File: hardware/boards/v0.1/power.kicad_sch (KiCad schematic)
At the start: 66 parts, among them IC3 SP3401-02UTG, J2 USB, U20 TPS62A02ADRLR, U23 BQ21040DBV, U30 FUSB307BVMPX, U31 TPS22929D, U32 LTC2942, U36 STM6601GU2BDM6F, U39 TPS61252DSG, U40 MIC2017YM6

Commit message: chore: schematic cleanup
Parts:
- D19: JLC (none) -> C130719
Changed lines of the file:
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@@
 			)
 		)
-		(property "JLC" ""
+		(property "JLC" "C130719"
 			(at 250.19 82.55 0)
 			(effects
@@
 					(size 1.27 1.27)
 				)
+				(hide yes)
 			)
 		)
@@
 				)
 				(justify left)
-			)
-		)
-		(property "MANUFACTURER" ""
-			(at 250.19 82.55 0)
-			(effects
-				(font
-					(size 1.27 1.27)
-				)
-			)
-		)
-		(property "MAXIMUM_PACKAGE_HEIGHT" ""
-			(at 250.19 82.55 0)
-			(effects
-				(font
-					(size 1.27 1.27)
-				)
-			)
-		)
-		(property "Connector" ""
-			(at 250.19 82.55 0)
-			(effects
-				(font
-					(size 1.27 1.27)
-				)
 			)
 		)
@@
 					(size 1.27 1.27)
 				)
-			)
-		)
+				(hide yes)
+			)
+		)

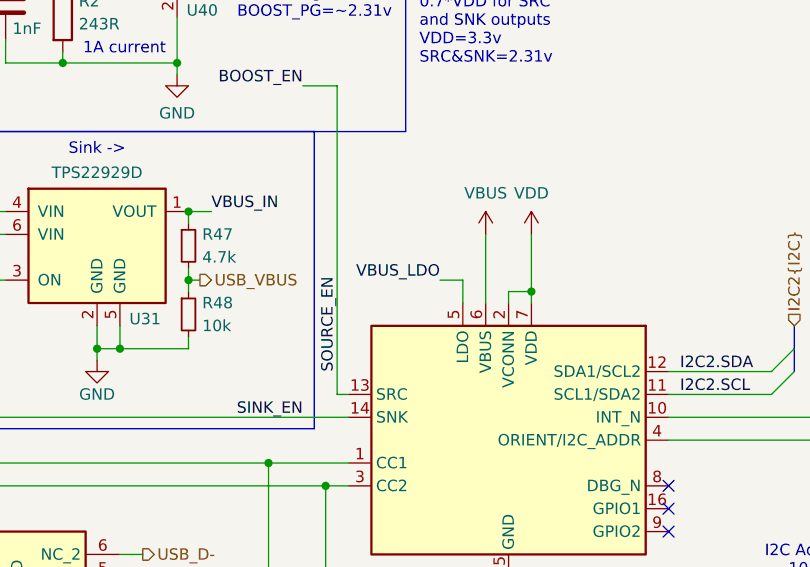
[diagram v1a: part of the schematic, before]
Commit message: feat: add LCD backlight control
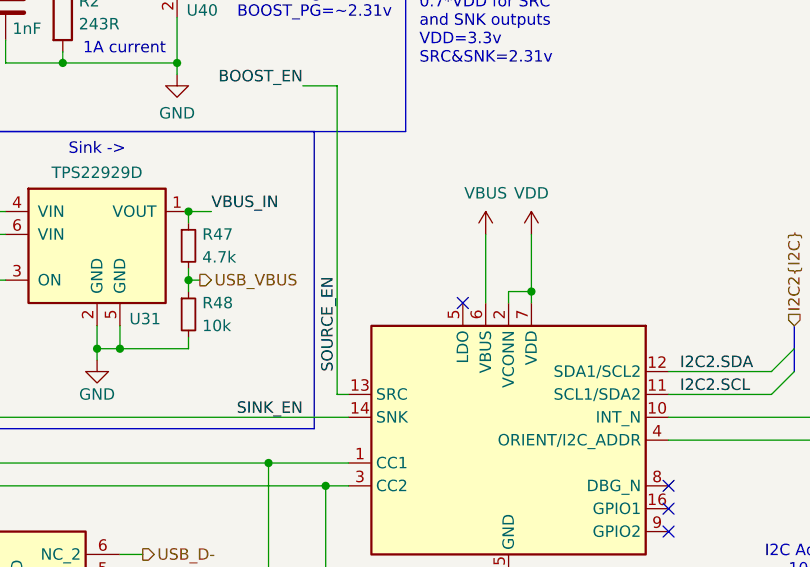
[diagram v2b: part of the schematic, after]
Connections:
- net VBUS_LDO: no longer names the net of U30.5 (LDO)
- no-connect marks 9 -> 10
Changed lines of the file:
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@@
 		(at 134.62 96.52)
+	)
+	(no_connect
+		(at 111.76 71.12)
 	)
 	(bus_entry
@@
 	(wire
 		(pts
-			(xy 109.22 68.58) (xy 111.76 68.58)
-		)
-		(stroke
-			(width 0)
-			(type default)
-		)
-	)
-	(wire
-		(pts
 			(xy 76.2 153.67) (xy 76.2 156.21)
 		)
@@
 		(pts
 			(xy 158.75 168.91) (xy 167.64 168.91)
-		)
-		(stroke
-			(width 0)
-			(type default)
-		)
-	)
-	(wire
-		(pts
-			(xy 111.76 71.12) (xy 111.76 68.58)
 		)
 		(stroke
@@
 		)
 	)
-	(label "VBUS_LDO"
-		(at 109.22 68.58 180)
-		(effects
-			(font
-				(size 1.27 1.27)
-			)
-			(justify right bottom)
-		)
-	)

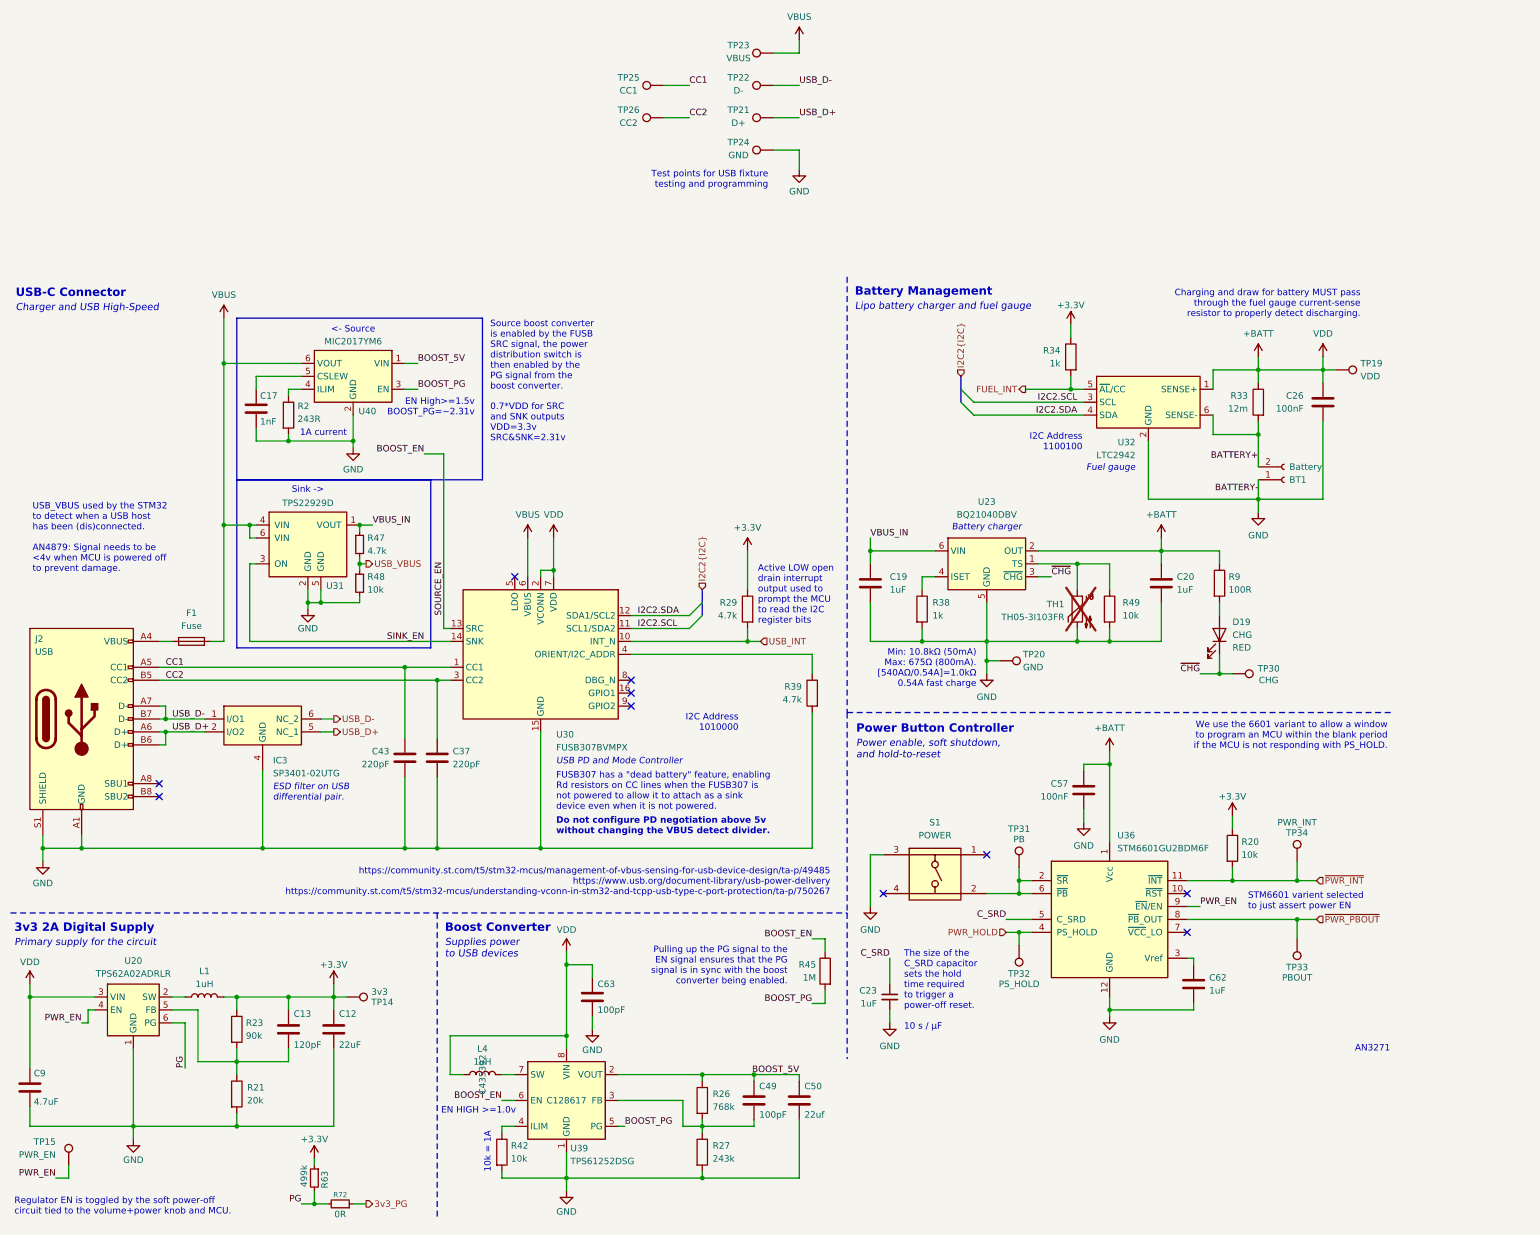
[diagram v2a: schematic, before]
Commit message: feat: add power LEDs and adjust layout
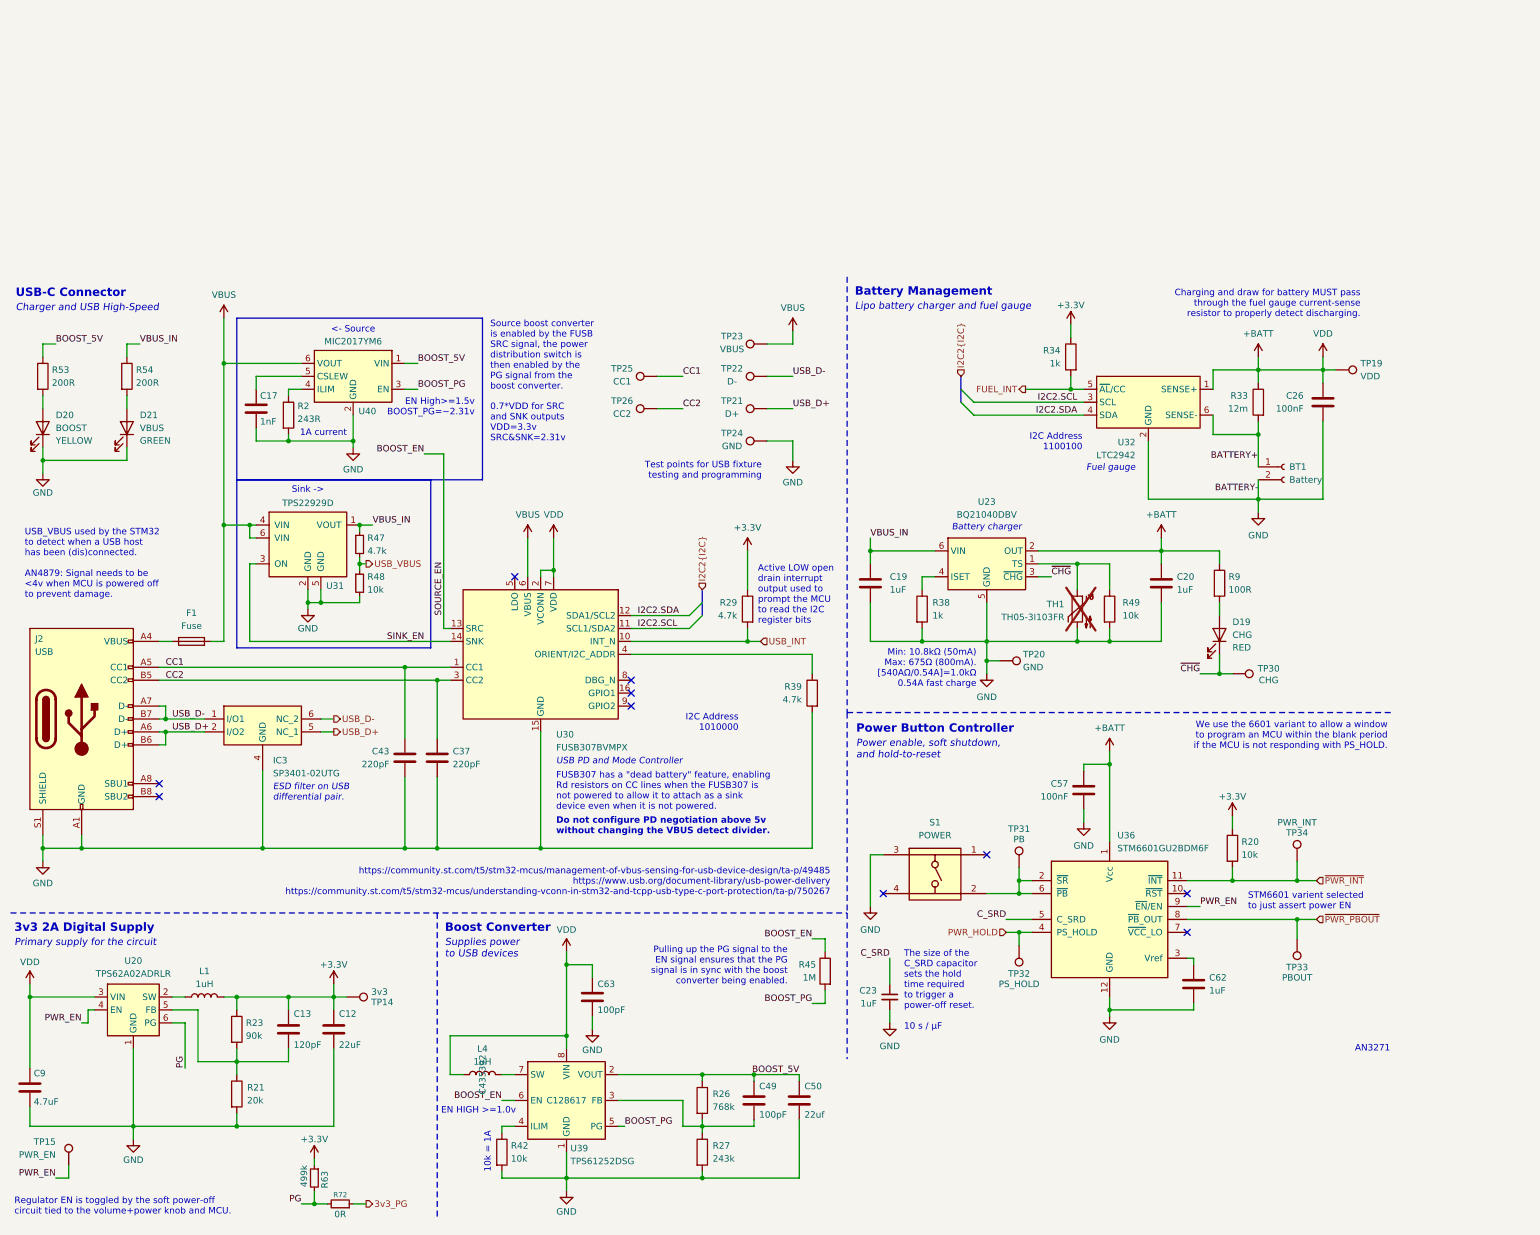
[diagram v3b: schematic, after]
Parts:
- added D20: BOOST, LED_SMD:LED_0805_2012Metric, symbol Device:LED
- added D21: VBUS, LED_SMD:LED_0805_2012Metric, symbol Device:LED
- added R53, R54: 200R, Resistor_SMD:R_0402_1005Metric, symbol Device:R
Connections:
- net BATTERY+: now also BT1.1 (Pin_1); no longer BT1.2 (Pin_2)
- net BOOST_5V: now also R53.1
- net GND: now also BT1.2 (Pin_2), D20.1 (K), D21.1 (K); no longer BT1.1 (Pin_1)
- net VBUS_IN: now also R54.1
- new net: D20.2 (A), R53.2
- new net: D21.2 (A), R54.2
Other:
- moved on the sheet: TP21, TP22, TP23, TP24, TP25, TP26

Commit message: feat: change charger, fuel gauge, and battery connector, re-route power system
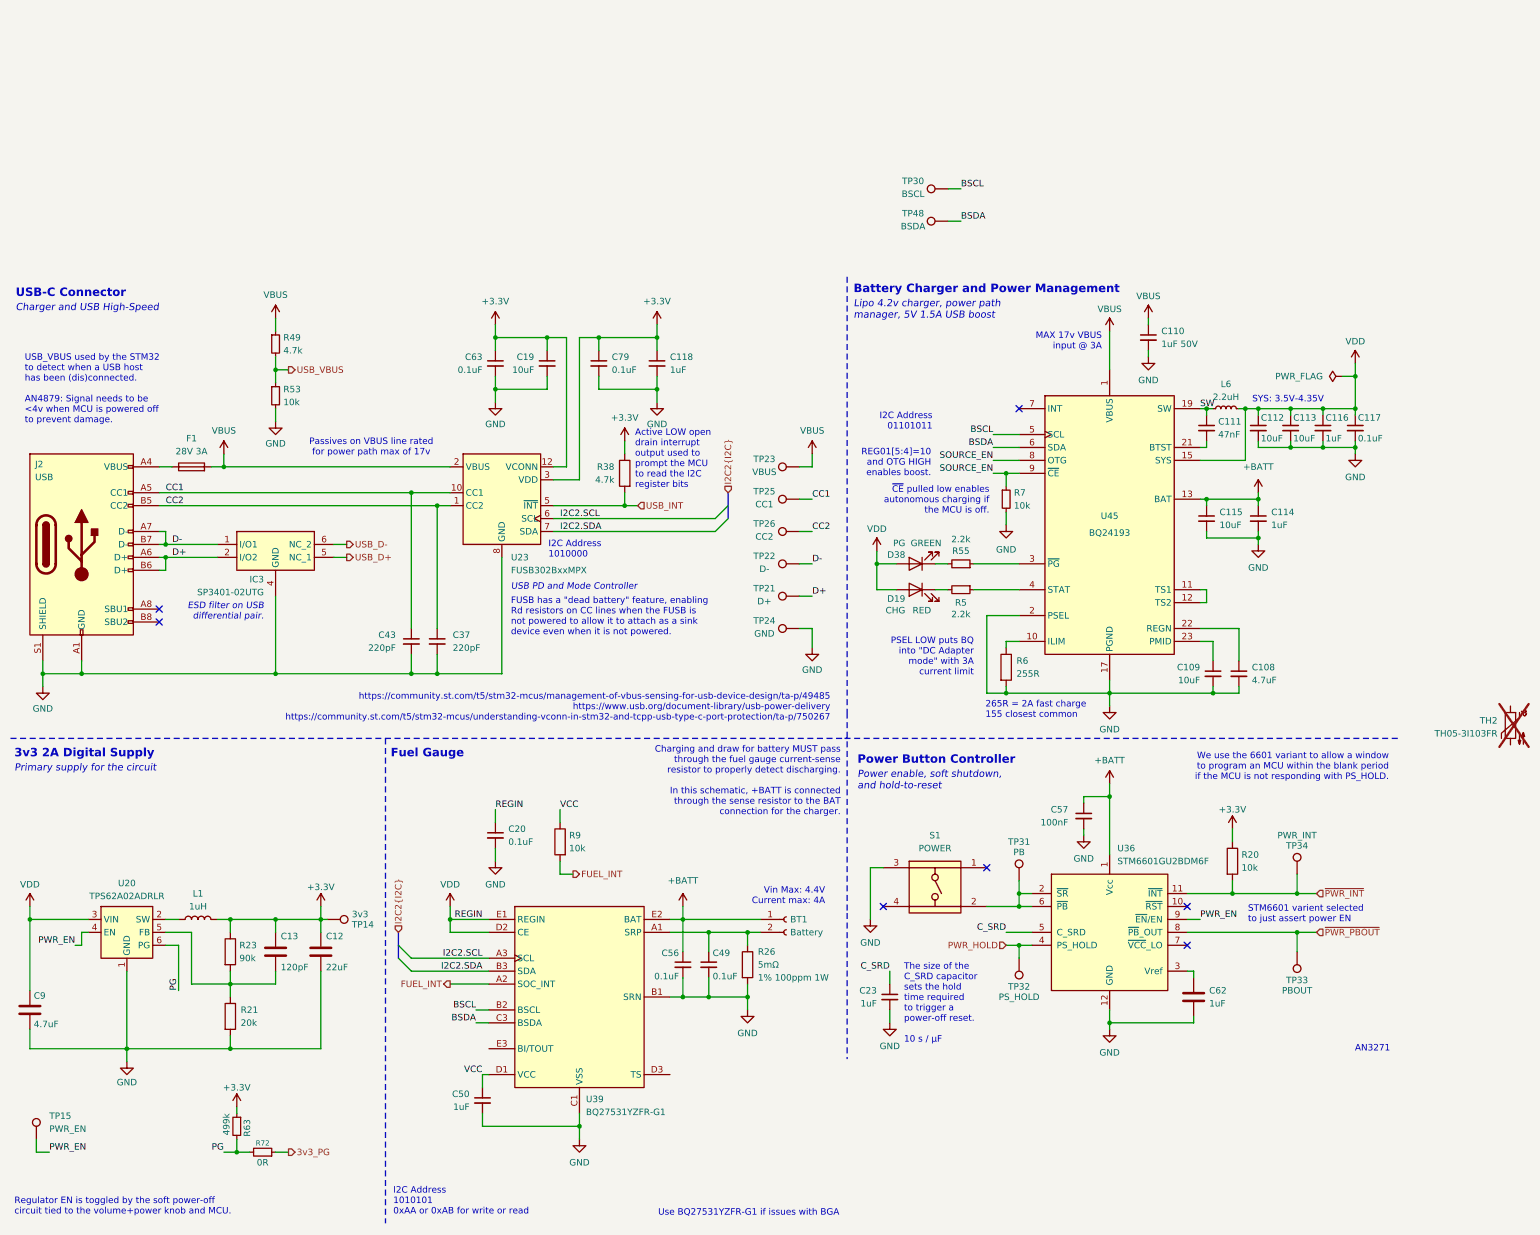
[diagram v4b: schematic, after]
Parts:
- removed C17: 1nF, Capacitor_SMD:C_0402_1005Metric, symbol Device:C
- removed C19, C20: 1uF, Capacitor_SMD:C_0805_2012Metric, symbol Device:C
- removed C26: 100nF, Capacitor_SMD:C_0603_1608Metric, symbol Device:C
- removed C49, C63: 100pF, Capacitor_SMD:C_0402_1005Metric, symbol Device:C
- removed C50: 22uf, Capacitor_SMD:C_0402_1005Metric, symbol Device:C
- removed D20: BOOST, LED_SMD:LED_0805_2012Metric, symbol Device:LED
- removed D21: VBUS, LED_SMD:LED_0805_2012Metric, symbol Device:LED
- removed L4: 1uH, Inductor_SMD:L_1008_2520Metric, symbol Device:L
- removed R2: 243R, Resistor_SMD:R_0402_1005Metric, symbol Device:R
- removed R27: 243k, Resistor_SMD:R_0402_1005Metric, symbol Device:R
- removed R29, R39: 4.7k, Resistor_SMD:R_0402_1005Metric, symbol Device:R
- removed R33: 12m, Resistor_SMD:R_1206_3216Metric_Pad1.30x1.75mm_HandSolder, symbol Device:R
- removed R34: 1k, Resistor_SMD:R_0603_1608Metric, symbol Device:R
- removed R42: 10k, Resistor_SMD:R_0402_1005Metric, symbol Device:R
- removed R45: 1M, Resistor_SMD:R_0402_1005Metric, symbol Device:R
- removed R47: 4.7k, Resistor_SMD:R_0402_1005Metric, symbol Device:R_Small
- removed R48: 10k, Resistor_SMD:R_0402_1005Metric, symbol Device:R_Small
- removed R49: 10k, Resistor_SMD:R_0805_2012Metric_Pad1.20x1.40mm_HandSolder, symbol Device:R
- removed R53, R54: 200R, Resistor_SMD:R_0402_1005Metric, symbol Device:R
- removed TH1: TH05-3I103FR, Resistor_SMD:R_0402_1005Metric_Pad0.72x0.64mm_HandSolder, symbol Device:Thermistor_NTC
- removed TP19: VDD, TestPoint:TestPoint_Pad_D1.0mm, symbol Connector:TestPoint
- removed TP20: GND, TestPoint:TestPoint_Pad_D1.0mm, symbol Connector:TestPoint
- removed U23: BQ21040DBV, Package_TO_SOT_SMD:SOT-23-6, symbol Battery_Management:BQ21040DBV
- removed U30: FUSB307BVMPX, Package_DFN_QFN:WQFN-16-1EP_3x3mm_P0.5mm_EP1.75x1.75mm, symbol Interface_USB:FUSB307BMPX
- removed U31: TPS22929D, Package_TO_SOT_SMD:SOT-23-6, symbol Power_Management:TPS22929D
- removed U32: LTC2942, Package_DFN_QFN:DFN-6-1EP_3x2mm_P0.5mm_EP1.65x1.35mm, symbol Battery_Management:LTC2942
- removed U39: TPS61252DSG, Package_SON:WSON-8-1EP_2x2mm_P0.5mm_EP0.9x1.6mm, symbol Regulator_Switching:TPS61252DSG
- removed U40: MIC2017YM6, Package_TO_SOT_SMD:SOT-23-6, symbol Power_Management:MIC2017YM6
- added C108: 4.7uF, Capacitor_SMD:C_0402_1005Metric, symbol Device:C_Small
- added C109, C112, C113, C115, C19: 10uF, Capacitor_SMD:C_0402_1005Metric, symbol Device:C_Small
- added C110: 1uF 50V, Capacitor_SMD:C_0603_1608Metric, symbol Device:C_Small
- added C111: 47nF, Capacitor_SMD:C_0402_1005Metric, symbol Device:C_Small
- added C114, C116, C118, C50: 1uF, Capacitor_SMD:C_0402_1005Metric, symbol Device:C_Small
- added C117, C20, C49, C56, C63, C79: 0.1uF, Capacitor_SMD:C_0402_1005Metric, symbol Device:C_Small
- added D38: PG, LED_SMD:LED_0805_2012Metric, symbol Device:LED
- added L6: 2.2uH, Inductor_SMD:L_0805_2012Metric, symbol Device:L_Small
- added R49: 4.7k, Resistor_SMD:R_0402_1005Metric, symbol Device:R_Small
- added R5, R55: 2.2k, Resistor_SMD:R_0402_1005Metric, symbol Device:R_Small
- added R53, R7: 10k, Resistor_SMD:R_0402_1005Metric, symbol Device:R_Small
- added R6: 255R, Resistor_SMD:R_0805_2012Metric_Pad1.20x1.40mm_HandSolder, symbol Device:R
- added TH2: TH05-3I103FR, Resistor_SMD:R_0402_1005Metric_Pad0.72x0.64mm_HandSolder, symbol Device:Thermistor_NTC
- added TP48: BSDA, TestPoint:TestPoint_Pad_D1.0mm, symbol Connector:TestPoint
- added U23: FUSB302BxxMPX, Package_DFN_QFN:WQFN-14-1EP_2.5x2.5mm_P0.5mm_EP1.45x1.45mm, symbol lethalbit:FUSB302B
- added U39: BQ27531YZFR-G1, pocket_synth:BGA15C50P3X5_196X261X63, symbol pocket_synth:BQ27531-G1
- added U45: BQ24193, Package_DFN_QFN:VQFN-24-1EP_4x4mm_P0.5mm_EP2.5x2.5mm_ThermalVias, symbol pocket_synth:BQ24193
- BT1: footprint Connector_JST:JST_PH_S2B-PH-SM4-TB_1x02-1MP_P2.00mm_Horizontal -> pocket_synth:CONN_2082940000-SD_02_MOL; JLC C295747 -> C19804046
- C23, C62: JLC C14445 -> C52923
- C37, C43, C57: symbol Device:C -> Device:C_Small
- D19: footprint LED_SMD:LED_0402_1005Metric -> LED_SMD:LED_0805_2012Metric; JLC C130719 -> C84256
- F1: value Fuse -> 28V 3A; JLC C20988 -> (none)
- R20: JLC C25531 -> C25744
- R26: value 768k -> 5mΩ; footprint Resistor_SMD:R_0402_1005Metric -> Resistor_SMD:R_1210_3225Metric; Characteristics (none) -> 1% 100ppm 1W; JLC C27017 -> C253508
- R38: value 1k -> 4.7k; JLC C11702 -> C25900
- R9: value 100R -> 10k; JLC C25076 -> C25744
- TP30: value CHG -> BSCL
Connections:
- net BATTERY+ is gone; now on net +BATT: BT1.1 (Pin_1)
- net +3.3V: now also R38.1, C118.1, C19.1, C63.1, C79.1, U23.12 (VCONN), U23.13 (VCONN), U23.3 (VDD), U23.4 (VDD)
- net +BATT: now also C114.1, C115.1, C56.1, U39.E2 (BAT), U45.13 (BAT), U45.14 (BAT); no longer C9.1, R9.1, U20.3 (VIN)
- net CC1: now also U23.10 (CC1), U23.11 (CC1)
- net CC2: now also U23.1 (CC2), U23.14 (CC2)
- net FUEL_INT: now also R9.2, U39.A2 (SOC_INT)
- net GND: now also R26.2, C108.2, C109.2, C110.2, C112.2, C113.2, C114.2, C115.2, C116.2, C117.2, C118.2, C19.2, C20.2, C49.2, C50.2, C56.2, C63.2, C79.2, R53.2, R6.2, R7.2, U23.15 (GND), U23.8 (GND), U23.9 (GND), U39.B1 (SRN), U39.C1 (VSS), U39.C2 (VSS), U45.17 (PGND), U45.18 (PGND), U45.2 (PSEL), U45.25 (PAD); no longer BT1.2 (Pin_2), R38.2
- net I2C2.SCL: now also U23.6 (SCL), U39.A3 (SCL)
- net I2C2.SDA: now also U23.7 (SDA), U39.B3 (SDA)
- net USB_D+: no longer IC3.2 (I/O2), J2.A6 (D+), J2.B6 (D+), TP21.1
- net USB_D-: no longer IC3.1 (I/O1), J2.A7 (D-), J2.B7 (D-), TP22.1
- net USB_INT: now also R38.2, U23.5 (~{INT})
- net USB_VBUS: now also R49.2, R53.1
- net VBUS: now also C110.1, R49.1, U23.2 (VBUS), U45.1 (VBUS), U45.24 (VBUS)
- net SYS: now reaches D19.2 (A)
- net SYS: now also C9.1, U20.3 (VIN), C112.1, C113.1, C116.1, C117.1, C20.1, D38.2 (A), L6.2, U39.D2 (CE), U39.E1 (REGIN), U45.15 (SYS), U45.16 (SYS); no longer R9.2
- net BOOST_5V: no longer names the net of R26.1
- net BOOST_5V: now also BT1.2 (Pin_2), C49.1, U39.A1 (SRP)
- net ~{CHG}: no longer names the net of D19.1 (K)
- net ~{CHG}: now also R5.2; no longer TP30.1
- new net: R6.1, U45.10 (ILIM)
- new net: U45.11 (TS1), U45.12 (TS2)
- new net: C111.2, U45.21 (BTST)
- new net: C108.1, U45.22 (REGN)
- new net: C109.1, U45.23 (PMID)
- new net: R55.1, U45.3 (~{PG})
- new net: R5.1, U45.4 (STAT)
- new net: D38.1 (K), R55.2
- new net BSCL: TP30.1, U39.B2 (BSCL), U45.5 (SCL)
- new net BSDA: TP48.1, U39.C3 (BSDA), U45.6 (SDA)
- new net D+: IC3.2 (I/O2), J2.A6 (D+), J2.B6 (D+), TP21.1
- new net D-: IC3.1 (I/O1), J2.A7 (D-), J2.B7 (D-), TP22.1
- new net SOURCE_EN: R7.1, U45.8 (OTG), U45.9 (~{CE})
- new net SW: C111.1, L6.1, U45.19 (SW), U45.20 (SW)
- new net VCC: C50.1, R9.1, U39.D1 (VCC)
- no-connect marks 10 -> 7
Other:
- note added: "265R = 2A fast charge 155 closest common"
- note added: "Battery Charger and Power Management"
- note added: "Charging and draw for battery MUST pass through the fuel gauge current-sense resistor to properly detect discharging. In this schematic, +BATT is connected through the sense resistor to the BAT connection for the charger."
- note added: "FUSB has a "dead battery" feature, enabling Rd resistors on CC lines when the FUSB is not powered to allow it to attach as a sink device even when it is not powered."
- note added: "Fuel Gauge"
- note added: "I2C Address 01101011"
- note added: "I2C Address 1010101 0xAA or 0xAB for write or read"
- note added: "Lipo 4.2v charger, power path manager, 5V 1.5A USB boost"
- note added: "MAX 17v VBUS input @ 3A"
- note added: "PSEL LOW puts BQ into "DC Adapter mode" with 3A current limit"
- note added: "Passives on VBUS line rated for power path max of 17v"
- note added: "REG01[5:4]=10 and OTG HIGH enables boost."
- note added: "SYS: 3.5V-4.35V"
- note added: "Use BQ27531YZFR-G1 if issues with BGA"
- note added: "Vin Max: 4.4V Current max: 4A"
- note added: "~{CE} pulled low enables autonomous charging if the MCU is off."
- note removed: "0.7*VDD for SRC and SNK outputs VDD=3.3v SRC&SNK=2.31v"
- note removed: "10k = 1A"
- note removed: "1A current"
- note removed: "<- Source"
- note removed: "Battery Management"
- note removed: "Battery charger"
- note removed: "Boost Converter"
- note removed: "Charging and draw for battery MUST pass through the fuel gauge current-sense resistor to properly detect discharging."
- note removed: "Do not configure PD negotiation above 5v without changing the VBUS detect divider."
- note removed: "EN HIGH >=1.0v"
- note removed: "EN High>=1.5v BOOST_PG=~2.31v"
- note removed: "FUSB307 has a "dead battery" feature, enabling Rd resistors on CC lines when the FUSB307 is not powered to allow it to attach as a sink device even when it is not powered."
- note removed: "Fuel gauge"
- note removed: "I2C Address 1100100"
- note removed: "Lipo battery charger and fuel gauge"
- note removed: "Min: 10.8kΩ (50mA) Max: 675Ω (800mA). [540AΩ/0.54A]=1.0kΩ 0.54A fast charge"
- note removed: "Pulling up the PG signal to the EN signal ensures that the PG signal is in sync with the boost converter being enabled."
- note removed: "Sink ->"
- note removed: "Source boost converter is enabled by the FUSB SRC signal, the power distribution switch is then enabled by the PG signal from the boost converter."
- note removed: "Supplies power to USB devices"
- note removed: "Test points for USB fixture testing and programming"
- moved on the sheet: BT1, C12, C13, C37, C43, C57, C62, C9, D19, F1, IC3, J2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
